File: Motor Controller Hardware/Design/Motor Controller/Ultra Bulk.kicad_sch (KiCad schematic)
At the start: 0 parts

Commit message: Arranged most footprints will route soon
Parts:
- added C141, C142, C143, C144, C163, C164, C165, C166, C167: 47u, Capacitor_SMD:CP_Elec_10x10, symbol Device:C_Polarized
- added C149, C172, C173, C174, C175, C176, C177, C178, C179, C180, C181, C182, C183, C184, C185, C186, C187, C188, C189, C190, C191, C192, C193, C194, C195, C196, C197, C198: 10u, Capacitor_SMD:C_1210_3225Metric, symbol Device:C
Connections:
- new net GNDPWR: C141.2, C142.2, C143.2, C144.2, C149.2, C163.2, C164.2, C165.2, C166.2, C167.2, C172.2, C173.2, C174.2, C175.2, C176.2, C177.2, C178.2, C179.2, C180.2, C181.2, C182.2, C183.2, C184.2, C185.2, C186.2, C187.2, C188.2, C189.2, C190.2, C191.2, C192.2, C193.2, C194.2, C195.2, C196.2, C197.2, C198.2
- new net V_{M}: C141.1, C142.1, C143.1, C144.1, C149.1, C163.1, C164.1, C165.1, C166.1, C167.1, C172.1, C173.1, C174.1, C175.1, C176.1, C177.1, C178.1, C179.1, C180.1, C181.1, C182.1, C183.1, C184.1, C185.1, C186.1, C187.1, C188.1, C189.1, C190.1, C191.1, C192.1, C193.1, C194.1, C195.1, C196.1, C197.1, C198.1

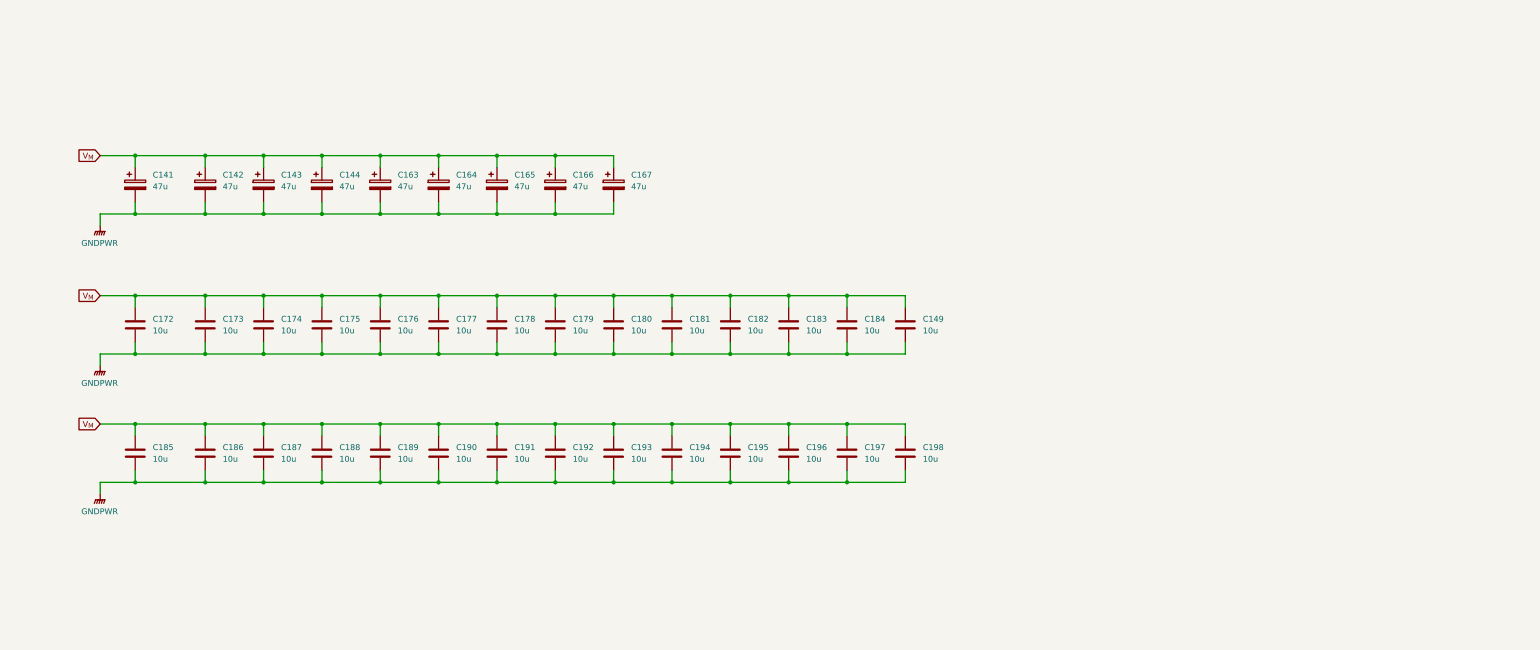
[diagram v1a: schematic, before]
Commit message: made some layout changes and started routing power stage
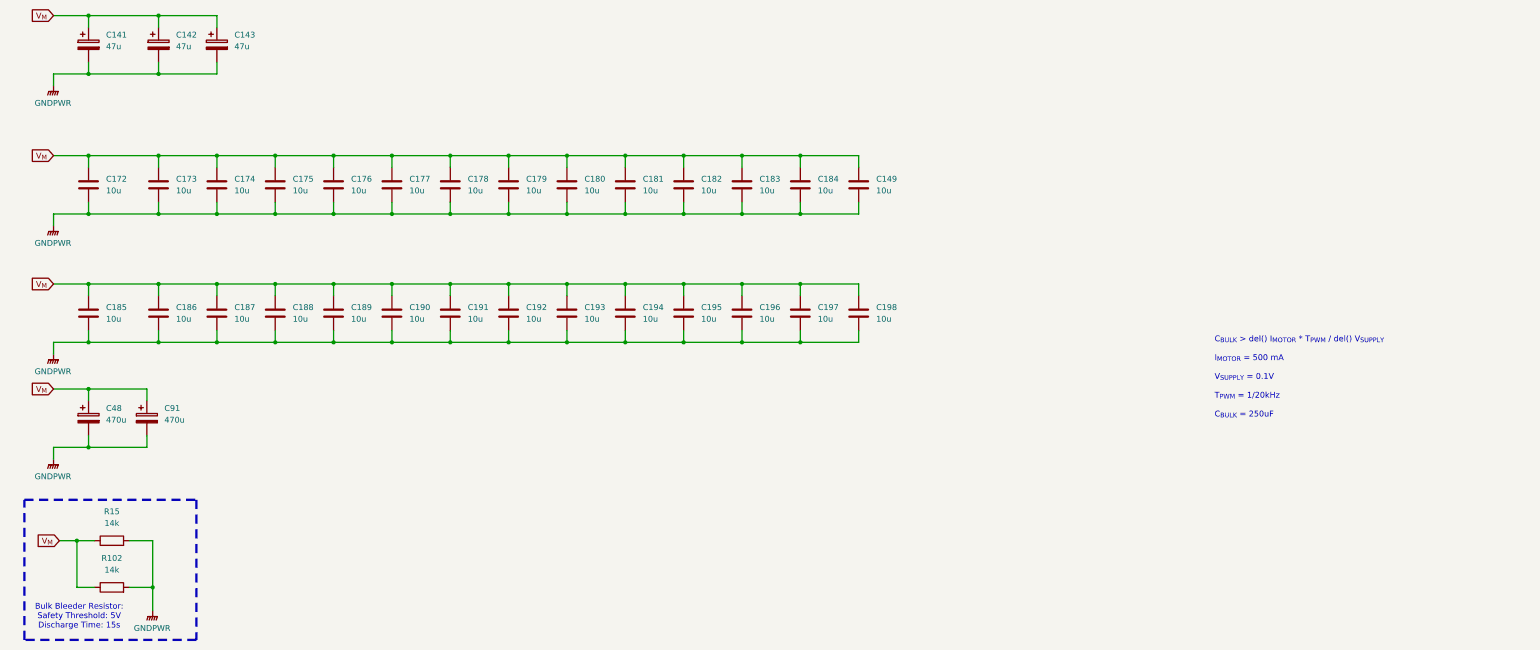
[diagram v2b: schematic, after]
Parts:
- removed C144, C163, C164, C165, C166, C167: 47u, Capacitor_SMD:CP_Elec_10x10, symbol Device:C_Polarized
- added C48, C91: 470u, Capacitor_THT:C_Radial_D16.0mm_H25.0mm_P7.50mm, symbol Device:C_Polarized
- added R102: 14k, Resistor_THT:R_Axial_DIN0617_L17.0mm_D6.0mm_P7.62mm_Vertical, symbol Device:R
- added R15: 14k, Resistor_SMD:R_1210_3225Metric, symbol Device:R
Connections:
- net GNDPWR: now also C48.2, C91.2, R102.2, R15.2
- net V_{M}: now also C48.1, C91.1, R102.1, R15.1
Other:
- note added: "Bulk Bleeder Resistor: Safety Threshold: 5V Discharge Time: 15s"
- note added: "C_{BULK} > del() I_{MOTOR} * T_{PWM} / del() V_{SUPPLY} I_{MOTOR} = 500 mA V_{SUPPLY} = 0.1V T_{PWM} = 1/20kHz C_{BULK} = 250uF"
- moved on the sheet: C141, C142, C143, C149, C172, C173, C174, C175, C176, C177, C178, C179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

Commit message: S
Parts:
- added C169: 10u, Capacitor_SMD:C_1210_3225Metric, symbol Device:C
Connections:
- net GNDPWR: now also C169.2
- net V_{M}: now also C169.1
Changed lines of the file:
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@@
 	)
 	(junction
+		(at 226.06 83.82)
+		(diameter 0)
+		(color 0 0 0 0)
+	)
+	(junction
 		(at 99.06 83.82)
 		(diameter 0)
@@
 	)
 	(junction
+		(at 226.06 96.52)
+		(diameter 0)
+		(color 0 0 0 0)
+	)
+	(junction
 		(at 200.66 68.58)
 		(diameter 0)
@@
 	(wire
 		(pts
+			(xy 238.76 86.36) (xy 238.76 83.82)
+		)
+		(stroke
+			(width 0)
+			(type default)
+		)
+	)
+	(wire
+		(pts
 			(xy 58.42 96.52) (xy 58.42 93.98)
 		)
@@
 	(wire
 		(pts
+			(xy 238.76 93.98) (xy 238.76 96.52)
+		)
+		(stroke
+			(width 0)
+			(type default)
+		)
+	)
+	(wire
+		(pts
 			(xy 213.36 96.52) (xy 213.36 93.98)
 		)
@@
 	(wire
 		(pts
+			(xy 226.06 96.52) (xy 238.76 96.52)
+		)
+		(stroke
+			(width 0)
+			(type default)
+		)
+	)
+	(wire
+		(pts
 			(xy 162.56 55.88) (xy 162.56 58.42)
 		)
@@
 	(wire
 		(pts
+			(xy 238.76 83.82) (xy 226.06 83.82)
+		)
+		(stroke
+			(width 0)
+			(type default)
+		)
+	)
+	(wire
+		(pts
 			(xy 71.12 109.22) (xy 71.12 106.68)
 		)
@@
 					(unit 1)
 				)
+			)
+		)
+	)
+	(symbol
+		(lib_id "Device:C")
+		(at 238.76 90.17 0)
+		(unit 1)
+		(exclude_from_sim no)
+		(in_bom yes)
+		(on_board yes)
+		(dnp no)
+		(fields_autoplaced yes)
+		(property "Reference" "C169"
+			(at 242.57 88.8999 0)
+			(effects
+				(font
+					(size 1.27 1.27)
+				)
+				(justify left)
+			)
+		)
+		(property "Value" "10u"
+			(at 242.57 91.4399 0)
+			(effects
+				(font
+					(size 1.27 1.27)
+				)
+				(justify left)
+			)
+		)
+		(property "Footprint" "Capacitor_SMD:C_1210_3225Metric"
+			(at 239.7252 93.98 0)
+			(effects
+				(font
+					(size 1.27 1.27)
+				)
+				(hide yes)
+			)
+		)
+		(property "Datasheet" "~"
+			(at 238.76 90.17 0)
+			(effects
+				(font
+					(size 1.27 1.27)
+				)
+				(hide yes)
+			)
+		)
+		(property "Description" "Unpolarized capacitor"
+			(at 238.76 90.17 0)
+			(effects
+				(font
+					(size 1.27 1.27)
+				)
+				(hide yes)
+			)
+		)
+		(property "LCSC Part#" ""
+			(at 238.76 90.17 0)
+			(effects
+				(font
+					(size 1.27 1.27)
+				)
+				(hide yes)
+			)
+		)
+		(pin "1"
+		)
+		(pin "2"
+		)
+		(instances
+			(project "Motor Controller"
+				(path "/480a1464-7c70-42e1-b2f7-69e659e11383/c39e9a42-301a-4d13-bc72-bf7c010c94d6/c7c24245-a02a-4ade-bdb7-97b8f980bfee"
+					(reference "C169")
+					(unit 1)
+				)

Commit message: A
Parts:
- removed C141, C142, C143: 47u, Capacitor_SMD:CP_Elec_10x10, symbol Device:C_Polarized
- added C82, C89: 470u, Capacitor_THT:C_Radial_D16.0mm_H25.0mm_P7.50mm, symbol Device:C_Polarized
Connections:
- net GNDPWR: now also C82.2, C89.2
- net V_{M}: now also C82.1, C89.1

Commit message: A
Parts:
- C82, C89: now not fitted; now left out of the parts list
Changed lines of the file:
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@@
 		(unit 1)
 		(exclude_from_sim no)
-		(in_bom yes)
-		(on_board yes)
-		(dnp no)
+		(in_bom no)
+		(on_board no)
+		(dnp yes)
 		(fields_autoplaced yes)
 		(property "Reference" "C82"
@@
 		(unit 1)
 		(exclude_from_sim no)
-		(in_bom yes)
-		(on_board yes)
-		(dnp no)
+		(in_bom no)
+		(on_board no)
+		(dnp yes)
 		(fields_autoplaced yes)
 		(property "Reference" "C89"

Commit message: A
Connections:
- net GNDPWR: now also R102.1; no longer R102.2
- net V_{M}: now also R102.2; no longer R102.1
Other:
- moved on the sheet: R102
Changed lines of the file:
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@@
 	(symbol
 		(lib_id "Device:R")
-		(at 63.5 149.86 90)
+		(at 63.5 149.86 270)
 		(unit 1)
 		(exclude_from_sim no)
@@
 		)
 		(property "Footprint" "Resistor_THT:R_Axial_DIN0617_L17.0mm_D6.0mm_P7.62mm_Vertical"
-			(at 63.5 151.638 90)
+			(at 63.5 148.082 90)
 			(effects
 				(font

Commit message: A
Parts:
- C149, C169, C172, C173, C174, C175, C176, C177, C178, C179, C180, C181, C182, C183, C184, C185, C186, C187, C188, C189, C190, C191, C192, C193, C194, C195, C196, C197, C198: LCSC# (none) -> C5156756
